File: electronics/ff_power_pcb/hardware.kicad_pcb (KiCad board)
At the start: 4 copper layers, 60 x 37 mm, 70 parts, among them J1 Conn_01x01_Female, J2 Conn_01x01_Female, U3 TPS62095RGTR, U4 TPS62095RGTR, U5 TPS62095RGTR, U6 TPS62095RGTR, U7 AP131-25

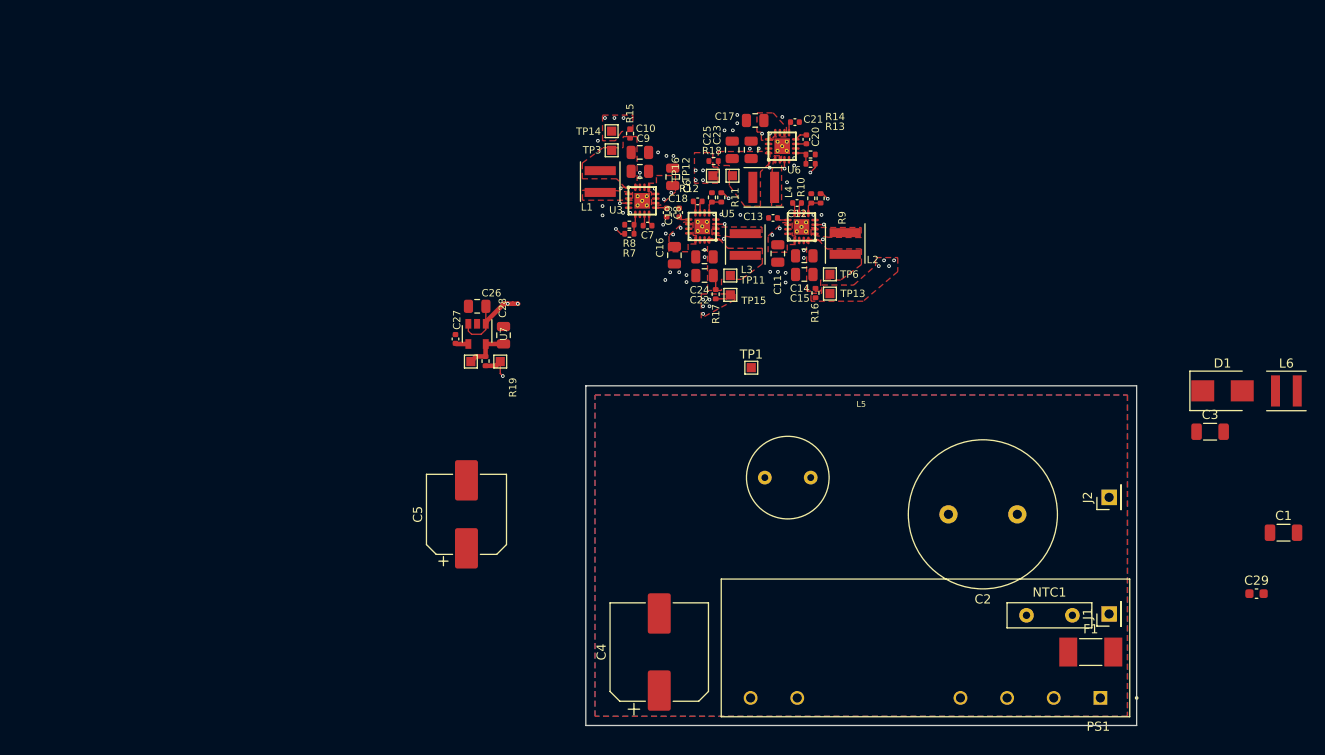
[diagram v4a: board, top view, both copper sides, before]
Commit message: Dropped in the power board with all the new components.
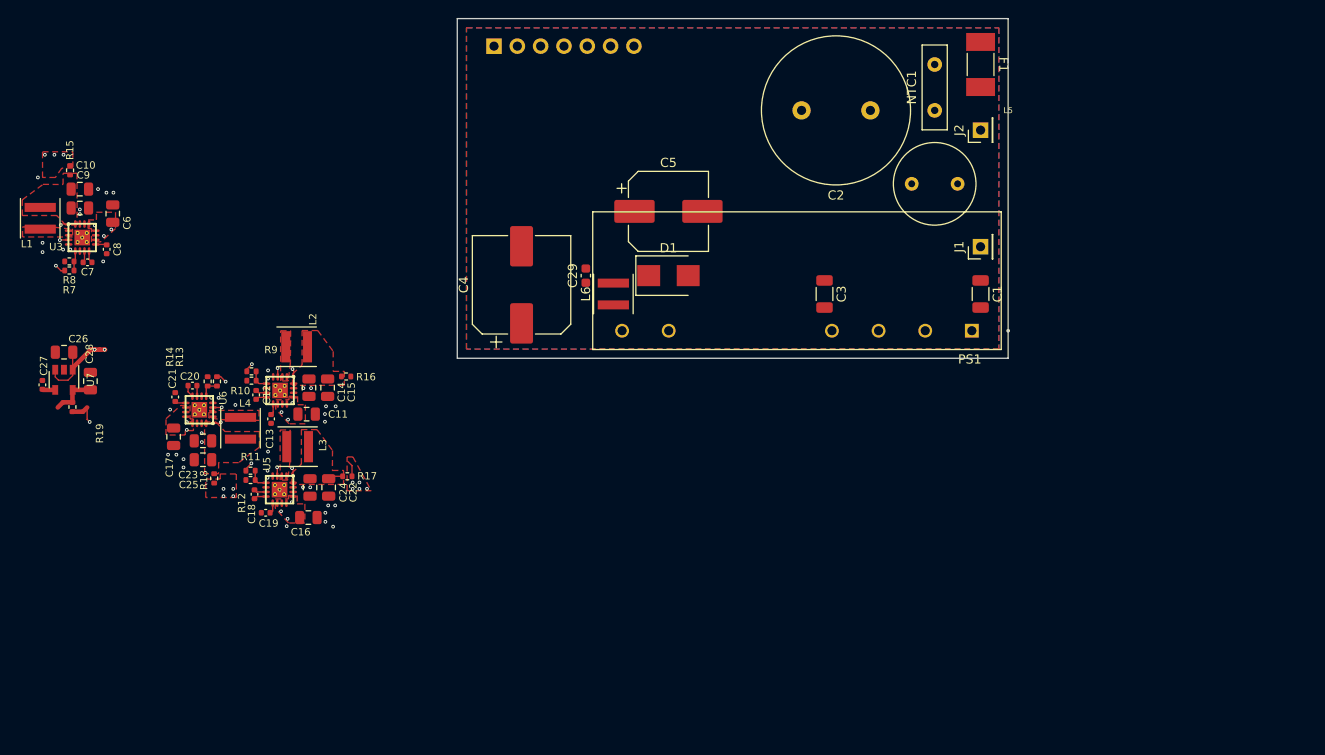
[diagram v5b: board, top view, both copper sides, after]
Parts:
- removed TP1, TP11, TP12, TP13, TP14, TP15, TP16, TP17, TP18, TP3, TP6: TestPoint, TestPoint:TestPoint_Pad_1.0x1.0mm
- added J3: Conn_01x07_Male, Connector_PinSocket_2.54mm:PinSocket_1x07_P2.54mm_Vertical, B.Cu at (90.0, 96.0)
- moved C29 80.9 mm to (100.0, 121.0), turned to 90 degrees
- moved L6 74.1 mm to (103.0, 123.0), turned to 90 degrees
- moved C21 73.8 mm to (55.3, 134.2), turned to 90 degrees
- moved C17 72.1 mm to (55.1, 138.6), turned to 270 degrees
- moved C20 72.0 mm to (57.2, 133.0), turned to 180 degrees
- moved R14 70.2 mm to (58.8, 132.5), turned to 90 degrees
- moved U6 69.7 mm to (57.9, 135.6), turned to 180 degrees
- moved R13 68.9 mm to (59.8, 132.5), turned to 270 degrees
- moved C23 67.6 mm to (58.3, 139.0), turned to 180 degrees
- moved C25 66.8 mm to (58.3, 141.1), turned to 180 degrees
- moved F1 65.1 mm to (143.0, 98.0), turned to 270 degrees
- moved R9 64.8 mm to (63.6, 131.4), turned to 0 degrees
- moved R18 64.5 mm to (59.5, 143.1), turned to 90 degrees
- moved R10 64.1 mm to (63.6, 132.4), turned to 180 degrees
- moved L4 62.7 mm to (62.4, 137.6), turned to 270 degrees
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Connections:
- J1 pad 1: /AC_L -> /AC_N
- J2 pad 1: /AC_N -> /AC_L
- R16 pad 1: +3V0 -> (no net)
- R19 pad 1: +2V5 -> (no net)
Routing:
- net (no net): track 0.00 -> 3.48 mm, vias 0 -> 1
- net +2V5: track 3.48 -> 0.00 mm, vias 1 -> 0
- net +3V0: vias 4 -> 0
- removed copper zone on F.Cu, net +3V0
